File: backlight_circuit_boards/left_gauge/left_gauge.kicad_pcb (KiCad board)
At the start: 2 copper layers, 95 x 86 mm, 14 parts, among them J1 IN, J2 OUT

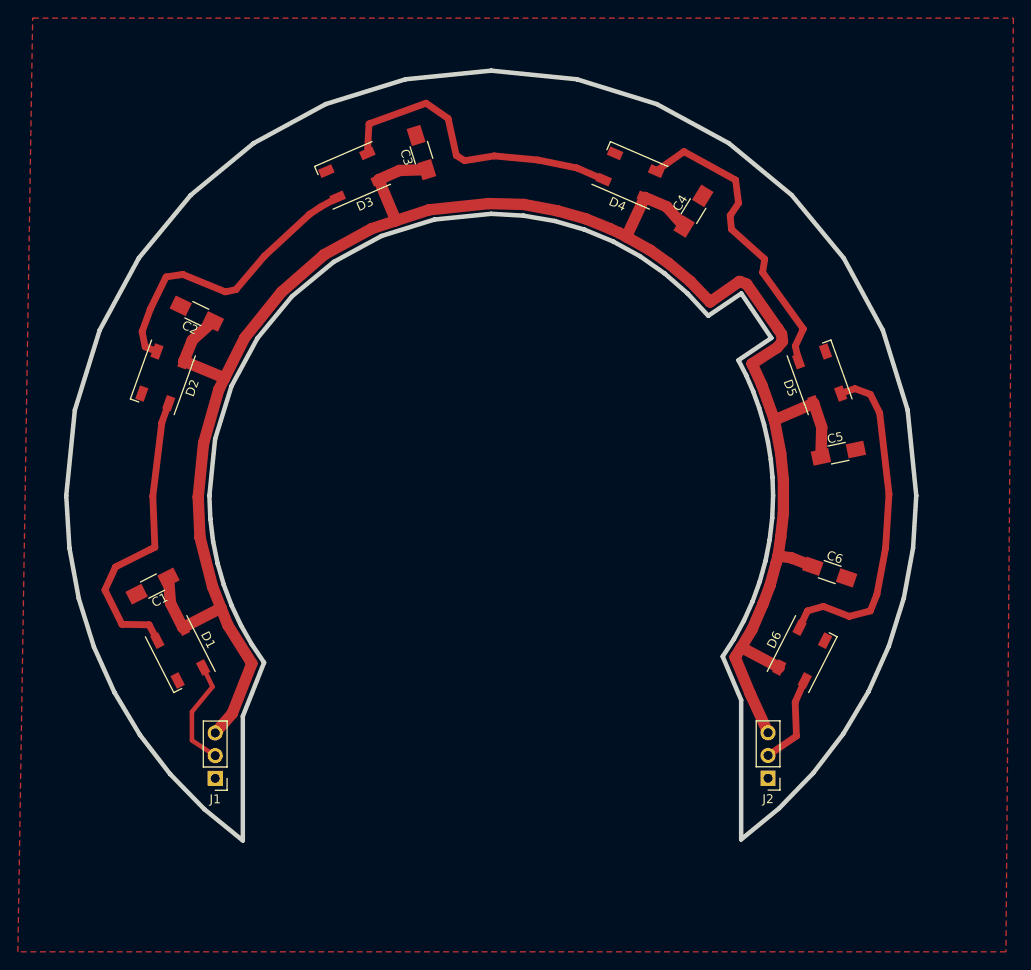
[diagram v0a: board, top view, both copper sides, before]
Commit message: Left gauge PCB done, WIP right gauge PCB, switched to KC 5
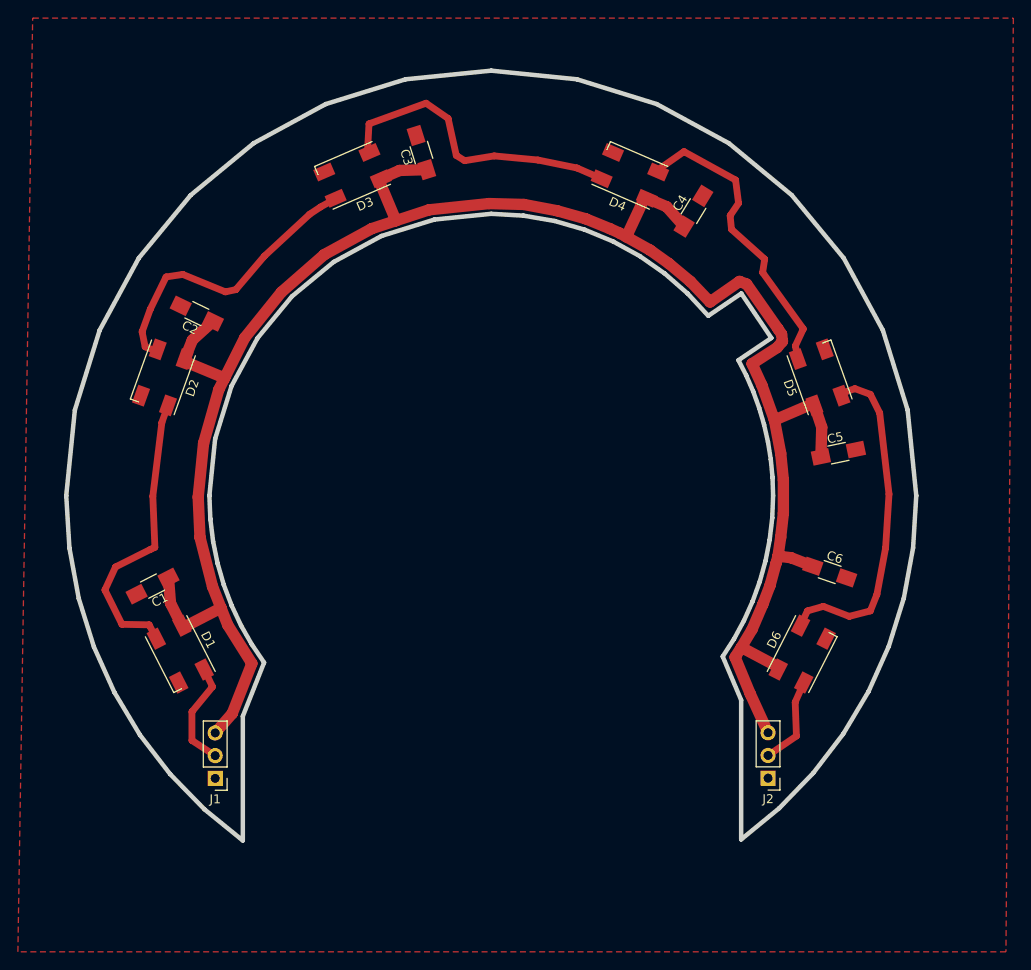
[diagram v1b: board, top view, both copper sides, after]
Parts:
- D1, D2, D3, D4, D5, D6: footprint LEDs:LED_WS2812B-PLCC4 -> Sparkfun LEDs:LED_WS2812B-PLCC4_HandSoldering

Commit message: improvements to all boards
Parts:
- added C7: 10 uF, Capacitors_Tantalum_SMD:CP_Tantalum_Case-D_EIA-7343-31_Reflow, F.Cu at (121.3, 82.5)
- J1, J2: footprint Pin_Headers:Pin_Header_Straight_1x03_Pitch2.54mm -> Frickelbude Connectors:wire_solder_pads_1x03_2.5x1.7mm_Pitch2.54mm
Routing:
- net VCC: track 230.4 -> 229.4 mm
